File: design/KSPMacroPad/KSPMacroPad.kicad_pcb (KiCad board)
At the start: 2 copper layers, 92 x 108.5 mm, 75 parts, among them SW1 SW_Push, SW10 SW_Push, SW11 SW_Push, SW12 SW_Push, SW13 SW_Push, SW14 SW_Push, SW15 SW_Push, SW16 SW_Push, SW2 SW_Push, SW3 SW_Push, SW4 SW_Push, SW5 SW_Push, SW6 SW_Push, SW7 SW_Push, SW8 SW_Push, SW9 SW_Push, U1 MOUDLE-SEEEDUINO-XIAO

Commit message: fixed wrong connection
encoder was connected to LED_GND
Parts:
- moved LED15 60.0 mm to (145.0, 110.0)
- moved LED16 60.0 mm to (145.0, 130.0)
- moved LED3 60.0 mm to (85.0, 110.0)
- moved LED4 60.0 mm to (85.0, 130.0)
- moved LED11 20.0 mm to (125.0, 110.0)
- moved LED12 20.0 mm to (125.0, 130.0)
- moved LED7 20.0 mm to (105.0, 110.0)
- moved LED8 20.0 mm to (105.0, 130.0)
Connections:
- ENCDR_RIGHT1 pad B: /LED_GND -> Net-(U1-PA7_A8_D8_SCK)
- U1 pad 9: /LED_GND -> Net-(U1-PA7_A8_D8_SCK)
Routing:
- net /LED_GND: track 551.1 -> 479.7 mm, vias 7 -> 8
- net Net-(LED19-DIN): track 19.9 -> 79.3 mm
- net Net-(LED2-DOUT): track 64.3 -> 26.7 mm, vias 0 -> 2
- net Net-(U1-PA7_A8_D8_SCK): track 0.00 -> 31.5 mm
- net Net-(LED11-DOUT): track 36.4 -> 15.4 mm
- net Net-(LED4-DIN): track 15.4 -> 34.7 mm
- net /LED_5V: track 531.3 -> 515.9 mm, vias 4 -> 13
- net Net-(LED15-DOUT): track 29.2 -> 44.1 mm
- net Net-(LED3-DOUT): track 30.2 -> 15.4 mm
- net Net-(LED12-DOUT): track 15.4 -> 28.1 mm
- net Net-(LED12-DIN): track 15.4 -> 28.1 mm
- net Net-(LED11-DIN): track 28.1 -> 15.4 mm
- net Net-(LED10-DOUT): track 28.3 -> 40.7 mm, vias 0 -> 4
- net Net-(D11-K): track 66.7 -> 75.8 mm, vias 2 -> 0
- net Net-(U1-PB09_A7_D7_RX): track 33.7 -> 41.7 mm
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
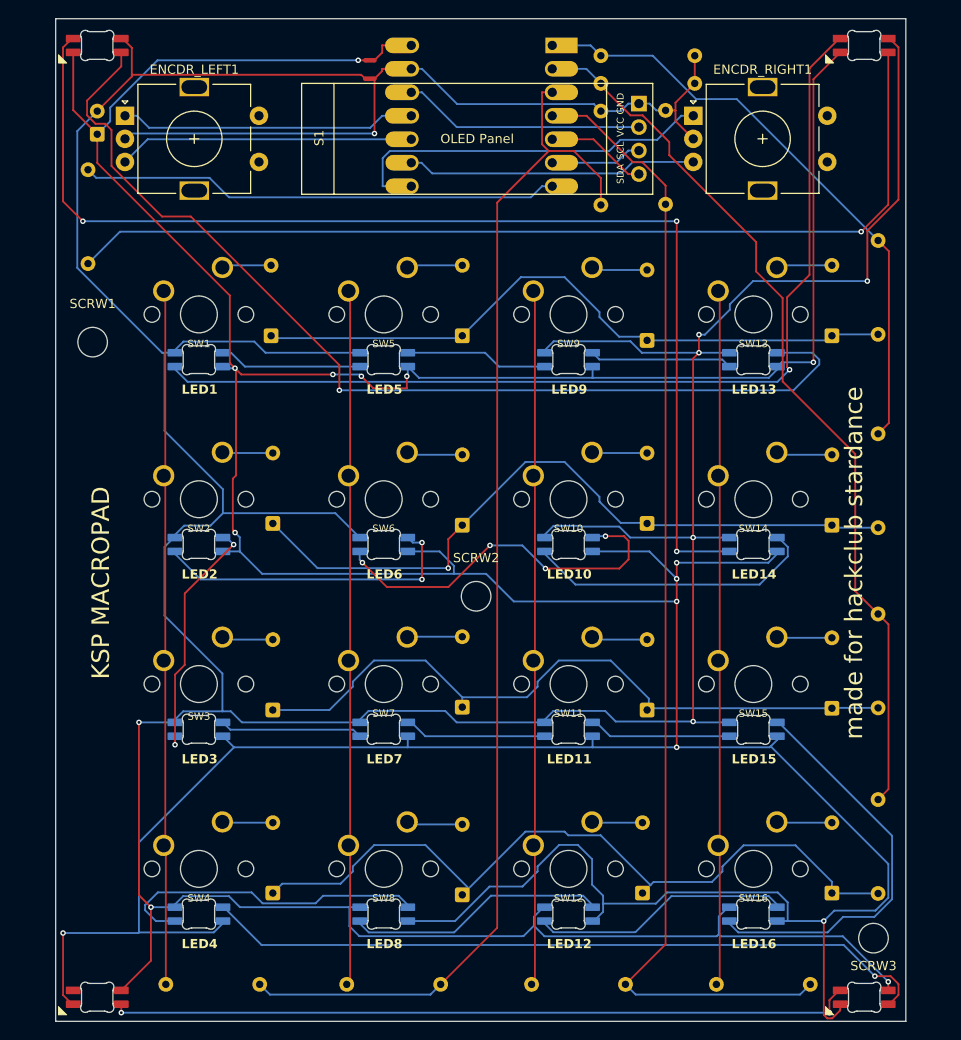
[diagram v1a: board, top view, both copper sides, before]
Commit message: Update PCB
fixed the sizing and made it match the schematic
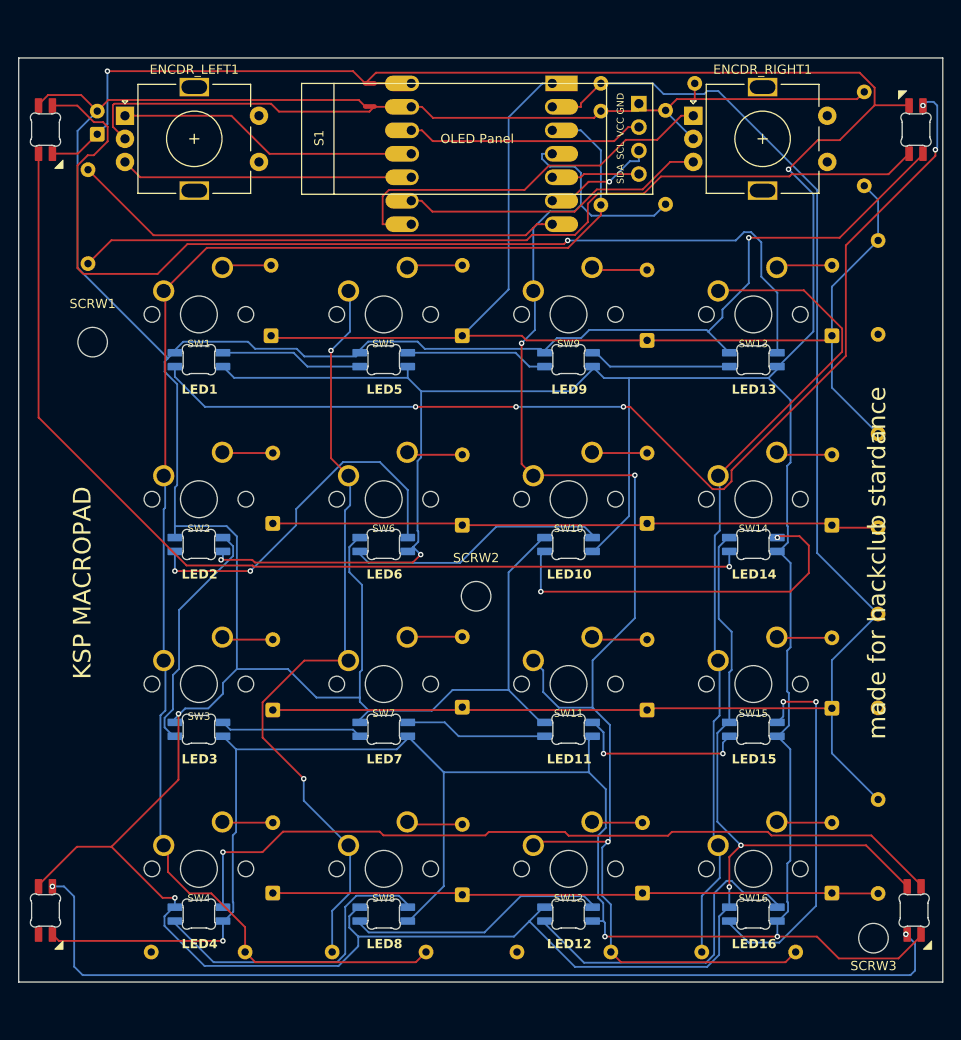
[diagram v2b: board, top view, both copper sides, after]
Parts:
- R2, R4: value 6.8k -> 10k
- R5, R7: value 6.8k -> 16k
- moved R9 18.8 mm to (157.0, 40.9), turned to -90 degrees
- moved LED19 11.0 mm to (162.5, 129.5), turned to -90 degrees
- moved LED20 11.0 mm to (68.5, 129.5), turned to -90 degrees
- moved LED17 10.5 mm to (162.5, 45.0), turned to 90 degrees
- moved LED18 10.5 mm to (68.5, 45.0), turned to -90 degrees
- moved U1 4.11 mm to (115.6, 47.6)
- moved R4 3.84 mm to (139.4, 134.0)
- moved R1 3.84 mm to (79.8, 134.0)
- moved R2 3.84 mm to (99.4, 134.0)
- moved R3 3.84 mm to (119.4, 134.0)
- moved NT1 3.00 mm to (103.5, 42.5)
- moved NT2 2.50 mm to (103.5, 40.0)
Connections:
- D1 pad 1: Net-(D1-K) -> /row1_2
- D11 pad 1: Net-(D11-K) -> /row3_4
- D13 pad 1: Net-(D1-K) -> /row1_2
- D15 pad 1: Net-(D11-K) -> /row3_4
- D3 pad 1: Net-(D11-K) -> /row3_4
- D5 pad 1: Net-(D1-K) -> /row1_2
- D7 pad 1: Net-(D11-K) -> /row3_4
- D9 pad 1: Net-(D1-K) -> /row1_2
- SW1 pad 1: Net-(R1-Pad1) -> /col1_2
- SW10 pad 1: Net-(R3-Pad1) -> /col3_4
- SW11 pad 1: Net-(R3-Pad1) -> /col3_4
- SW12 pad 1: Net-(R3-Pad1) -> /col3_4
- SW2 pad 1: Net-(R1-Pad1) -> /col1_2
- SW3 pad 1: Net-(R1-Pad1) -> /col1_2
- SW4 pad 1: Net-(R1-Pad1) -> /col1_2
- SW9 pad 1: Net-(R3-Pad1) -> /col3_4
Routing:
- net Net-(D11-K): track 75.8 -> 0.00 mm
- net Net-(R3-Pad1): track 75.7 -> 0.00 mm
- net Net-(R1-Pad1): track 75.6 -> 0.00 mm
- net Net-(D1-K): track 71.9 -> 0.00 mm
- net /row3_4: track 97.5 -> 168.7 mm
- net /row1_2: track 65.9 -> 124.9 mm
- net /col3_4: track 124.6 -> 159.3 mm, vias 0 -> 3
- net /col1_2: track 133.1 -> 161.7 mm
- net Net-(LED19-DOUT): track 80.5 -> 106.5 mm
- net /LED_5V: track 515.9 -> 493.3 mm, vias 13 -> 7
- net Net-(D12-K): track 82.0 -> 65.7 mm
- net Net-(LED14-DIN): track 126.9 -> 111.6 mm, vias 3 -> 1
- net /an_GND: track 79.5 -> 94.6 mm, vias 1 -> 0
- net Net-(R4-Pad1): track 75.7 -> 90.0 mm
- net Net-(LED10-DOUT): track 40.7 -> 28.2 mm, vias 4 -> 0
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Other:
- board size 92 x 108.5 mm -> 100 x 100 mm

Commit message: actually matches schematic
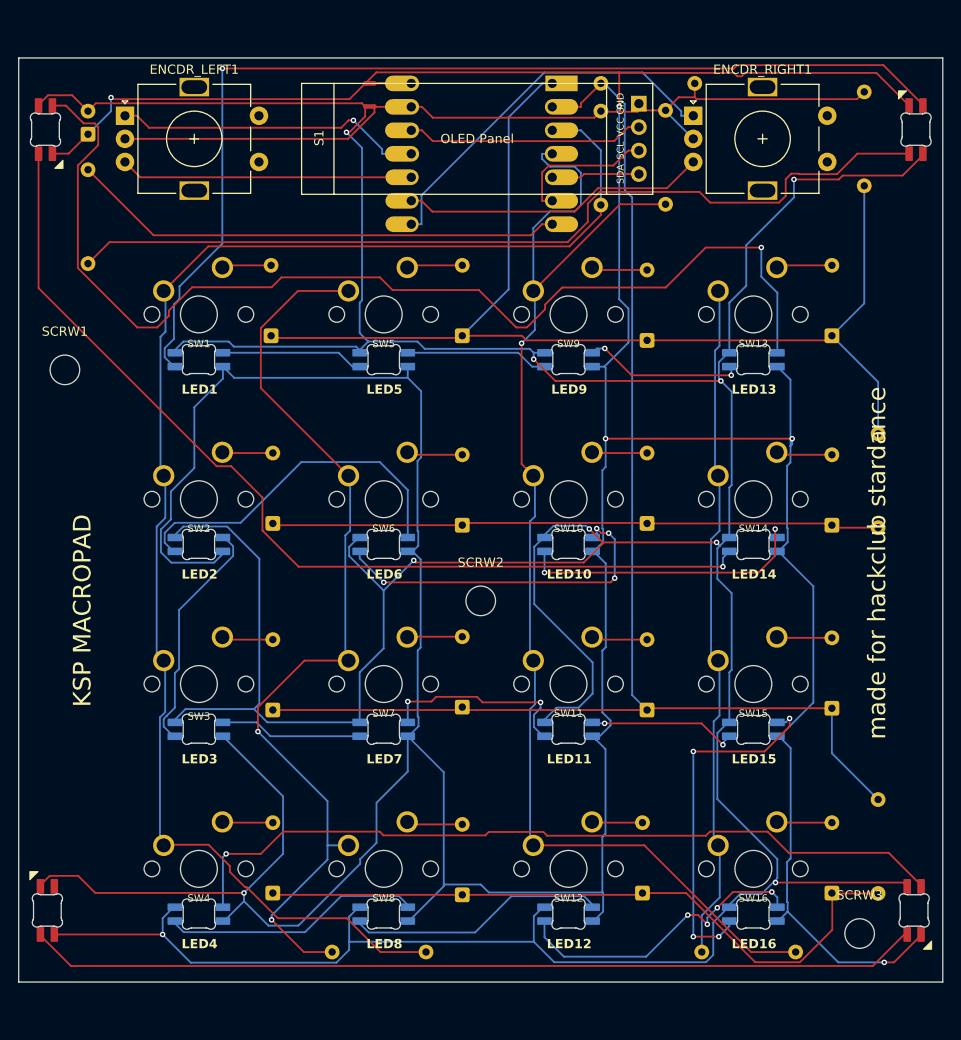
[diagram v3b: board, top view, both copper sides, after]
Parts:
- removed R1, R3, R6, R8: 22k, Resistor_THT:R_Axial_DIN0207_L6.3mm_D2.5mm_P10.16mm_Horizontal
- moved SCRW1 4.24 mm to (70.5, 71.0)
- moved SCRW3 1.58 mm to (156.5, 132.0)
- moved C1 1.00 mm to (73.0, 45.5)
- moved SCRW2 0.71 mm to (115.5, 96.0)
- turned LED20 to 90 degrees
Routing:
- net /LED_5V: track 493.3 -> 518.6 mm, vias 7 -> 6
- net /col3_4: track 159.3 -> 136.4 mm, vias 3 -> 1
- net /row3_4: track 168.7 -> 149.4 mm
- net Net-(R2-Pad1): track 85.1 -> 102.3 mm
- net Net-(R4-Pad1): track 90.0 -> 74.1 mm
- net Net-(LED19-DOUT): track 106.5 -> 96.7 mm, vias 2 -> 0
- net Net-(LED10-DIN): track 41.2 -> 31.9 mm
- net Net-(LED10-DOUT): track 28.2 -> 37.4 mm, vias 0 -> 4
- net /LED_GND: track 479.8 -> 488.9 mm, vias 5 -> 9
- net Net-(D12-K): track 65.7 -> 74.2 mm
- net Net-(LED14-DIN): track 111.6 -> 105.1 mm
- net Net-(LED13-DOUT): track 113.2 -> 119.5 mm
- net Net-(LED11-DIN): track 15.4 -> 21.6 mm, vias 0 -> 2
- net Net-(LED4-DIN): track 33.8 -> 28.1 mm
- net Net-(LED1-DIN): track 118.5 -> 113.2 mm, vias 5 -> 1
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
